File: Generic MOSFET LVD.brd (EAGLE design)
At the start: 41.9 x 38.1 mm, 14 parts, among them IC1 TINY13-20PU, Q1 IRF520

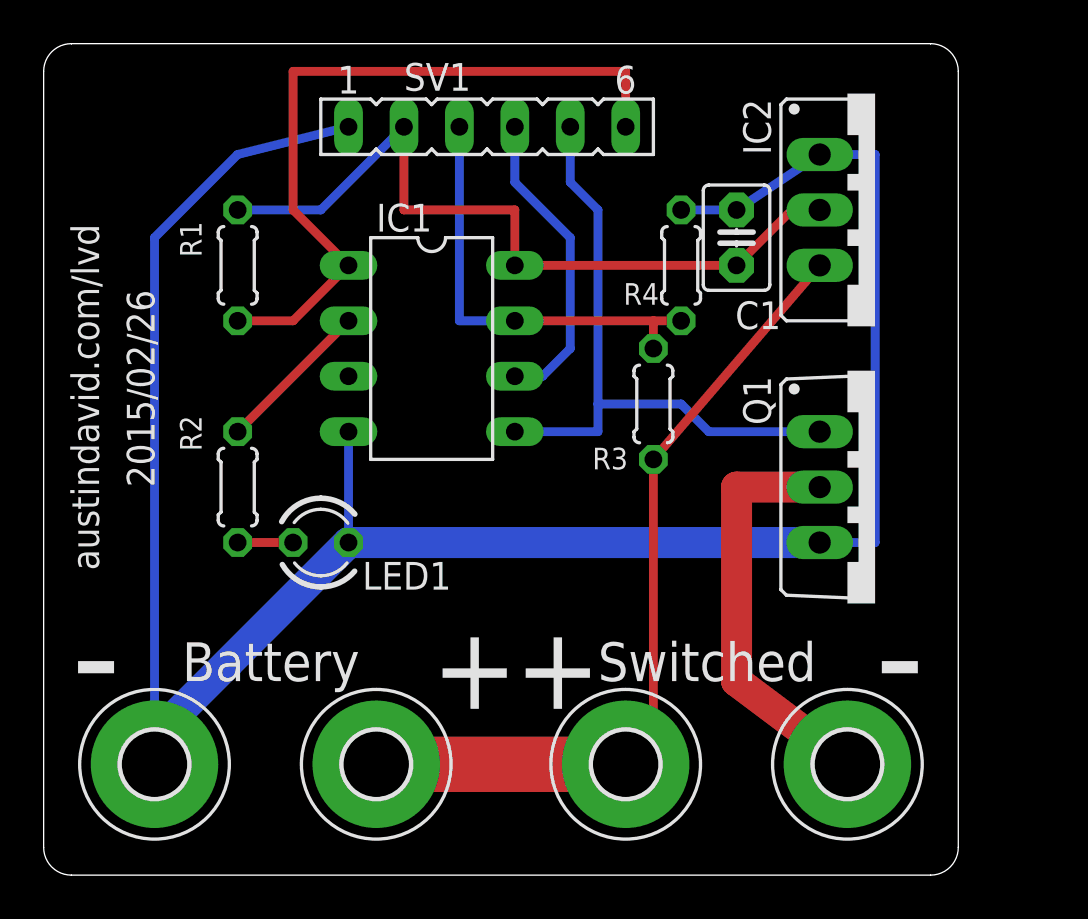
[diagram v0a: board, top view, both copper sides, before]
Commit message: new 4/10 LVD
Smaller, with a built-in pushbutton.  Dropped the 6-pin debugging
header.
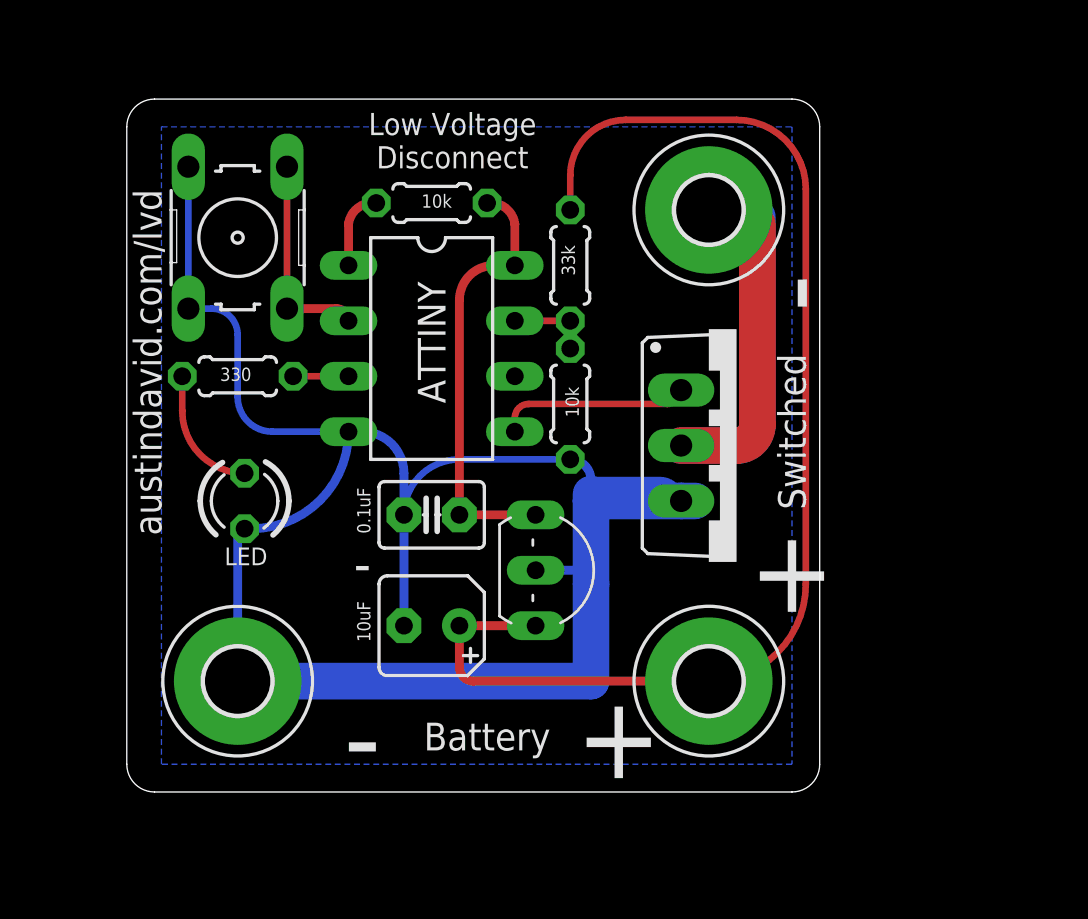
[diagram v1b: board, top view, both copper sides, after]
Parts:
- removed IC2: (no value), v-reg:78XXS
- removed LED1: TLLR4400, led:LED3MM
- removed SV1: (no value), con-lsta:FE06
- removed V_SWITCHED: MOUNT-PAD-ROUND3.0, holes:3,0-PAD
- added C2: 0.1uF, capacitor-wima:C2.5-3
- added LED: TLLR4400, led:LED3MM
- added Q2: 2N5484, transistor-fet:TO92-
- added S1: (no value), switch-omron:B3F-10XX
- C1: value 0.1uF -> 10uF; device capacitor-wima:C2.5-3 -> rcl:B45181A
- R2: value 470 -> 330
- moved GND_SWITCHED 26.2 mm to (62.2, 48.3)
- moved C1 22.6 mm to (49.5, 29.2), turned to 180 degrees
- moved V_BATT 15.7 mm to (62.2, 26.7)
- moved R1 9.34 mm to (49.5, 48.6), turned to 180 degrees
- moved R4 8.13 mm to (55.9, 39.4), turned to 90 degrees
- moved R3 7.41 mm to (55.9, 45.7), turned to 270 degrees
- moved Q1 6.63 mm to (63.5, 37.5)
- moved GND_BATT 5.39 mm to (40.6, 26.7)
- moved R2 5.08 mm to (40.6, 40.6), turned to 180 degrees
- renumbered IC1 to ATTINY
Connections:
- removed net LED_SIGNAL: ATTINY.2, R2.1
- removed net N$5: ATTINY.5, Q1.G, SV1.5
- removed net N$6: ATTINY.6, SV1.4
- new net BUTTON: ATTINY.2, S1.1, S1.2
- new net LED: ATTINY.3, R2.1
- new net NC: ATTINY.6
- new net RELAY: ATTINY.5, Q1.G
- net GND: now also C1.-, C2.2, LED.K, Q2.2, S1.3, S1.4; no longer C1.2, IC2.IN, LED1.K, SV1.1
- net N$1: no longer SV1.6
- net N$4: now also LED.A; no longer LED1.A
- net VCC: now also C2.1, Q2.3; no longer C1.1, IC2.GND, SV1.2
- net V_BATT: now also C1.+, Q2.1; no longer IC2.OUT, V_SWITCHED.B3,0
- net V_SENSE: no longer SV1.3
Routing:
- net N$1: track 33.9 -> 3.49 mm
- net N$5: track 29.0 -> 0.00 mm
- net V_BATT: track 35.8 -> 56.2 mm
- net V_SENSE: track 20.3 -> 3.81 mm
- net GND: track 104.0 -> 89.4 mm
- net VCC: track 34.4 -> 20.0 mm
- net N$6: track 14.3 -> 0.00 mm
- net GND_SWITCHED: track 19.1 -> 31.3 mm
- net BUTTON: track 0.00 -> 9.55 mm
- net RELAY: track 0.00 -> 8.78 mm
- net LED_SIGNAL: track 7.18 -> 0.00 mm
- net N$4: track 2.54 -> 5.63 mm
- net LED: track 0.00 -> 2.54 mm
- added copper zone on layer 16, net GND
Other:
- board size 41.9 x 38.1 mm -> 31.8 x 31.8 mm
- board text added: "2016-04-10"
- board text added: "Low Voltage Disconnect"
- board text removed: "2015/02/26"
